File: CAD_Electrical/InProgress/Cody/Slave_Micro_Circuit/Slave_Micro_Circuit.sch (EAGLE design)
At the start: 22 parts, among them IC1 ATMEGA88A-PU, IC2 TS12A4515P, IC3 TS12A4515P, IC4 TS12A4515P, J1 22-23-2061, Y1 16MHz

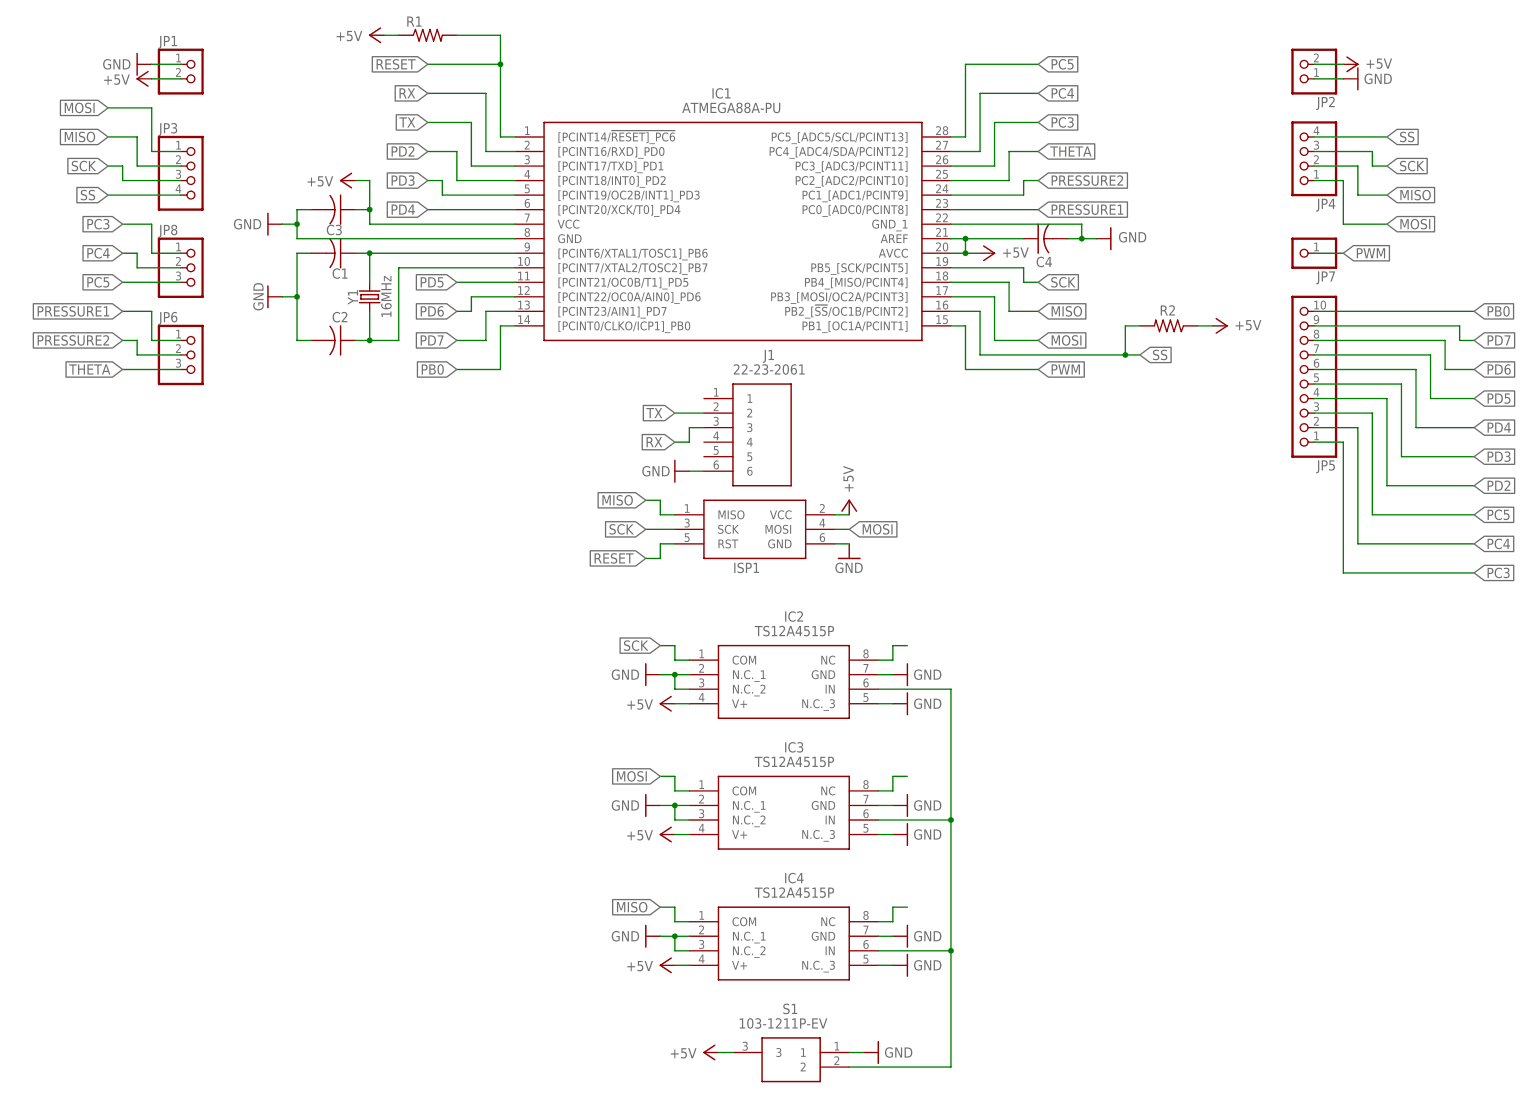
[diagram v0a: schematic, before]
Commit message: Created slave micro Eagle component.
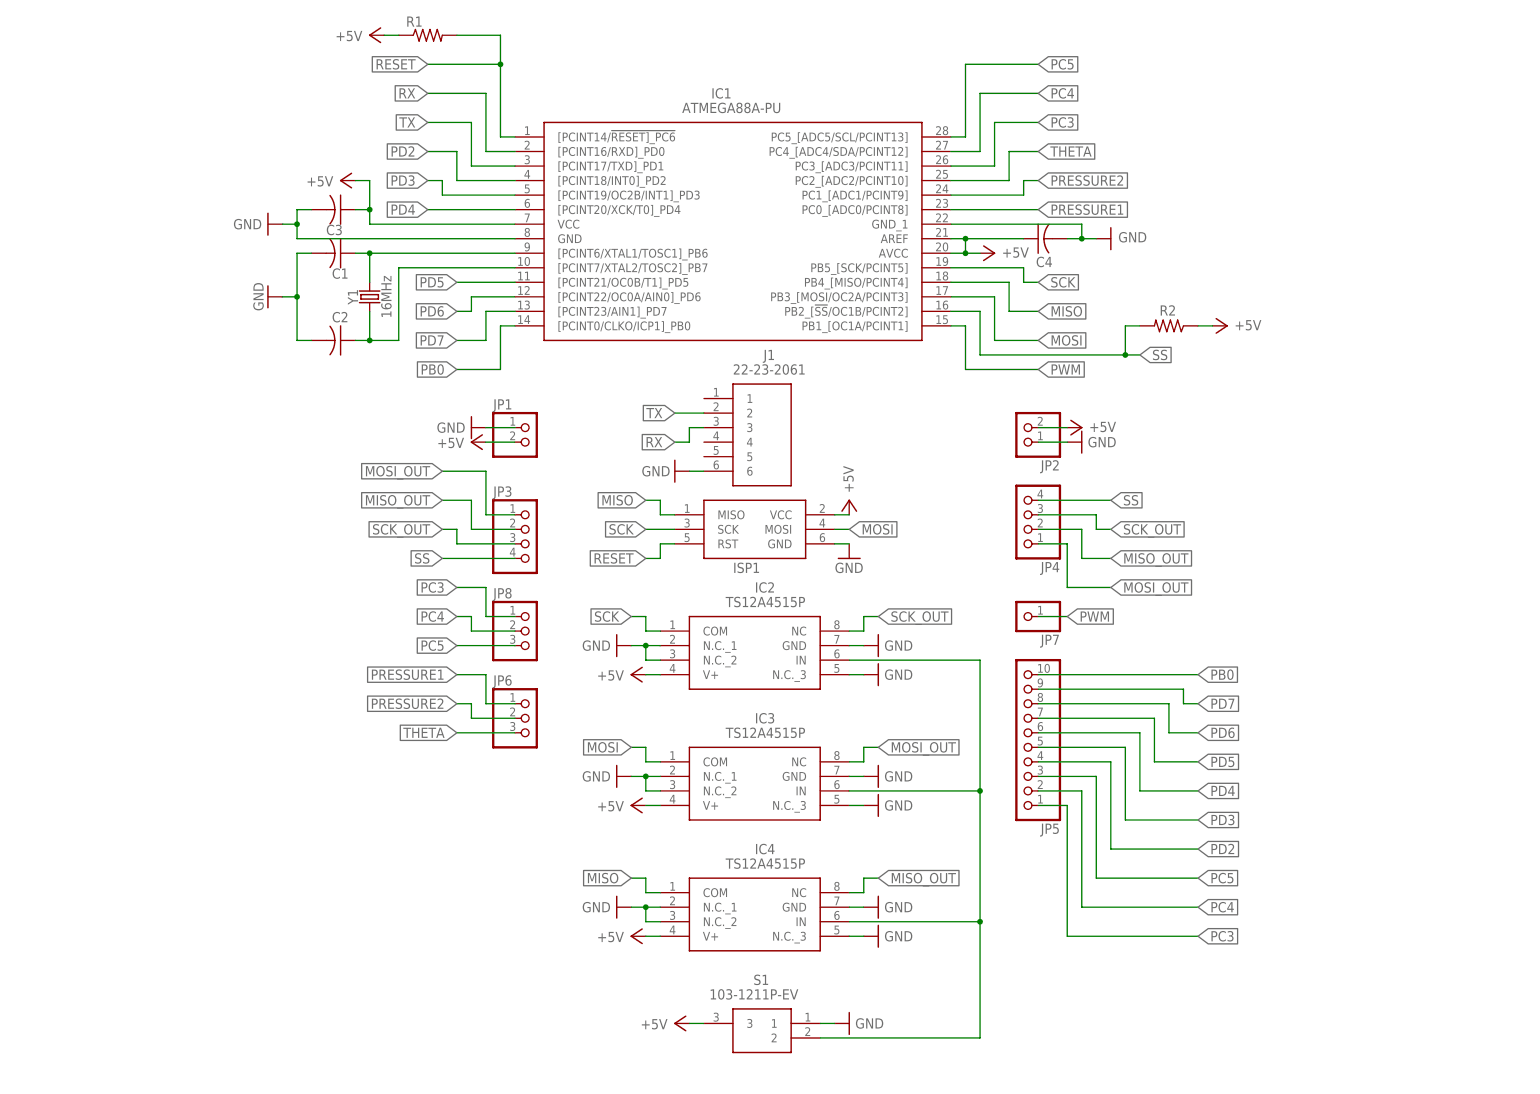
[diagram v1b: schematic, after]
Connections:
- removed net N$2: IC2.NC
- removed net N$3: IC3.NC
- removed net N$4: IC4.NC
- new net MISO_OUT: IC4.NC, JP3.2, JP4.2
- new net MOSI_OUT: IC3.NC, JP3.1, JP4.1
- new net SCK_OUT: IC2.NC, JP3.3, JP4.3
- net MISO: no longer JP3.2, JP4.2
- net MOSI: no longer JP3.1, JP4.1
- net SCK: no longer JP3.3, JP4.3
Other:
- moved on the sheet: IC2, IC3, IC4, JP1, JP2, JP3, JP4, JP5, JP6, JP7, JP8, S1
